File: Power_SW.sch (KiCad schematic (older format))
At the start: 96 parts, among them J9 2057-PH1-04-UA-ND, Q10 FDMS7608S, Q11 FDMS7608S, Q12 FDMS7608S, Q13 FDMS7608S, Q26 BC847BV, Q27 BC847BV, U35 XRP7724ILB-F, U36 NCP186AMX180TAG, U37 NCP186AMX120TAG

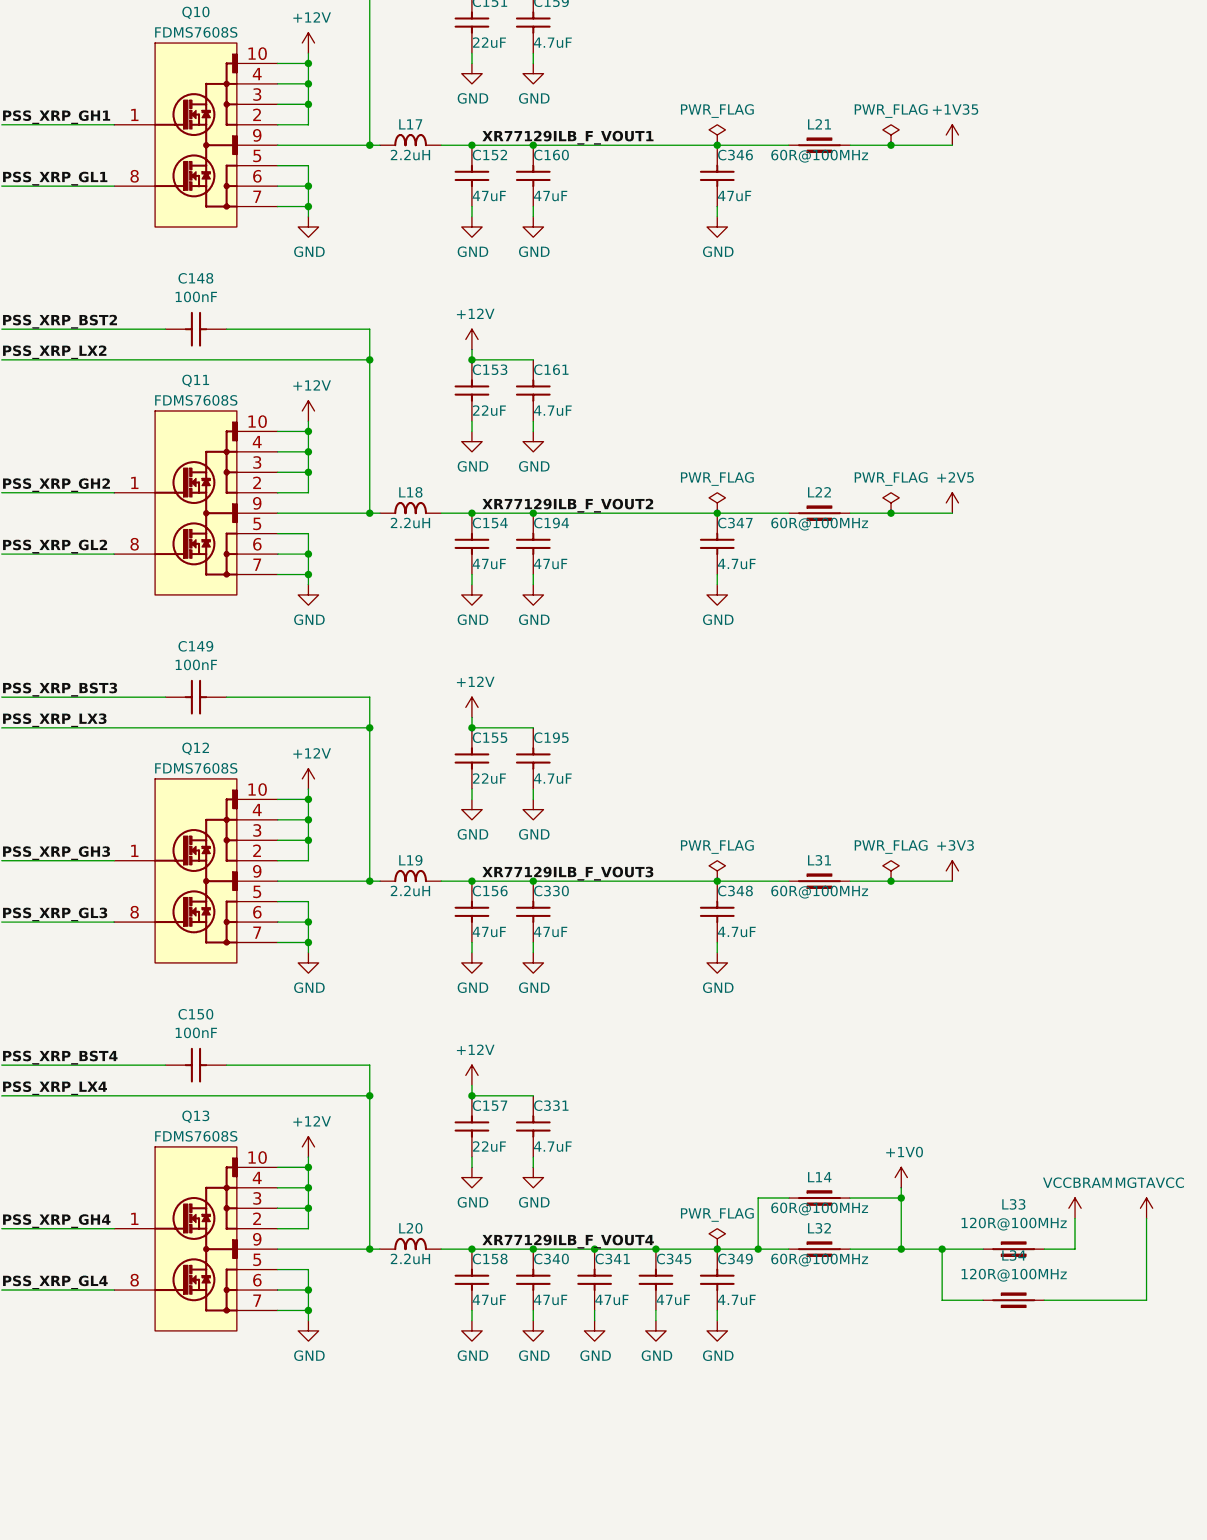
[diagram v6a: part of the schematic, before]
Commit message: added netlist to .xdc converter
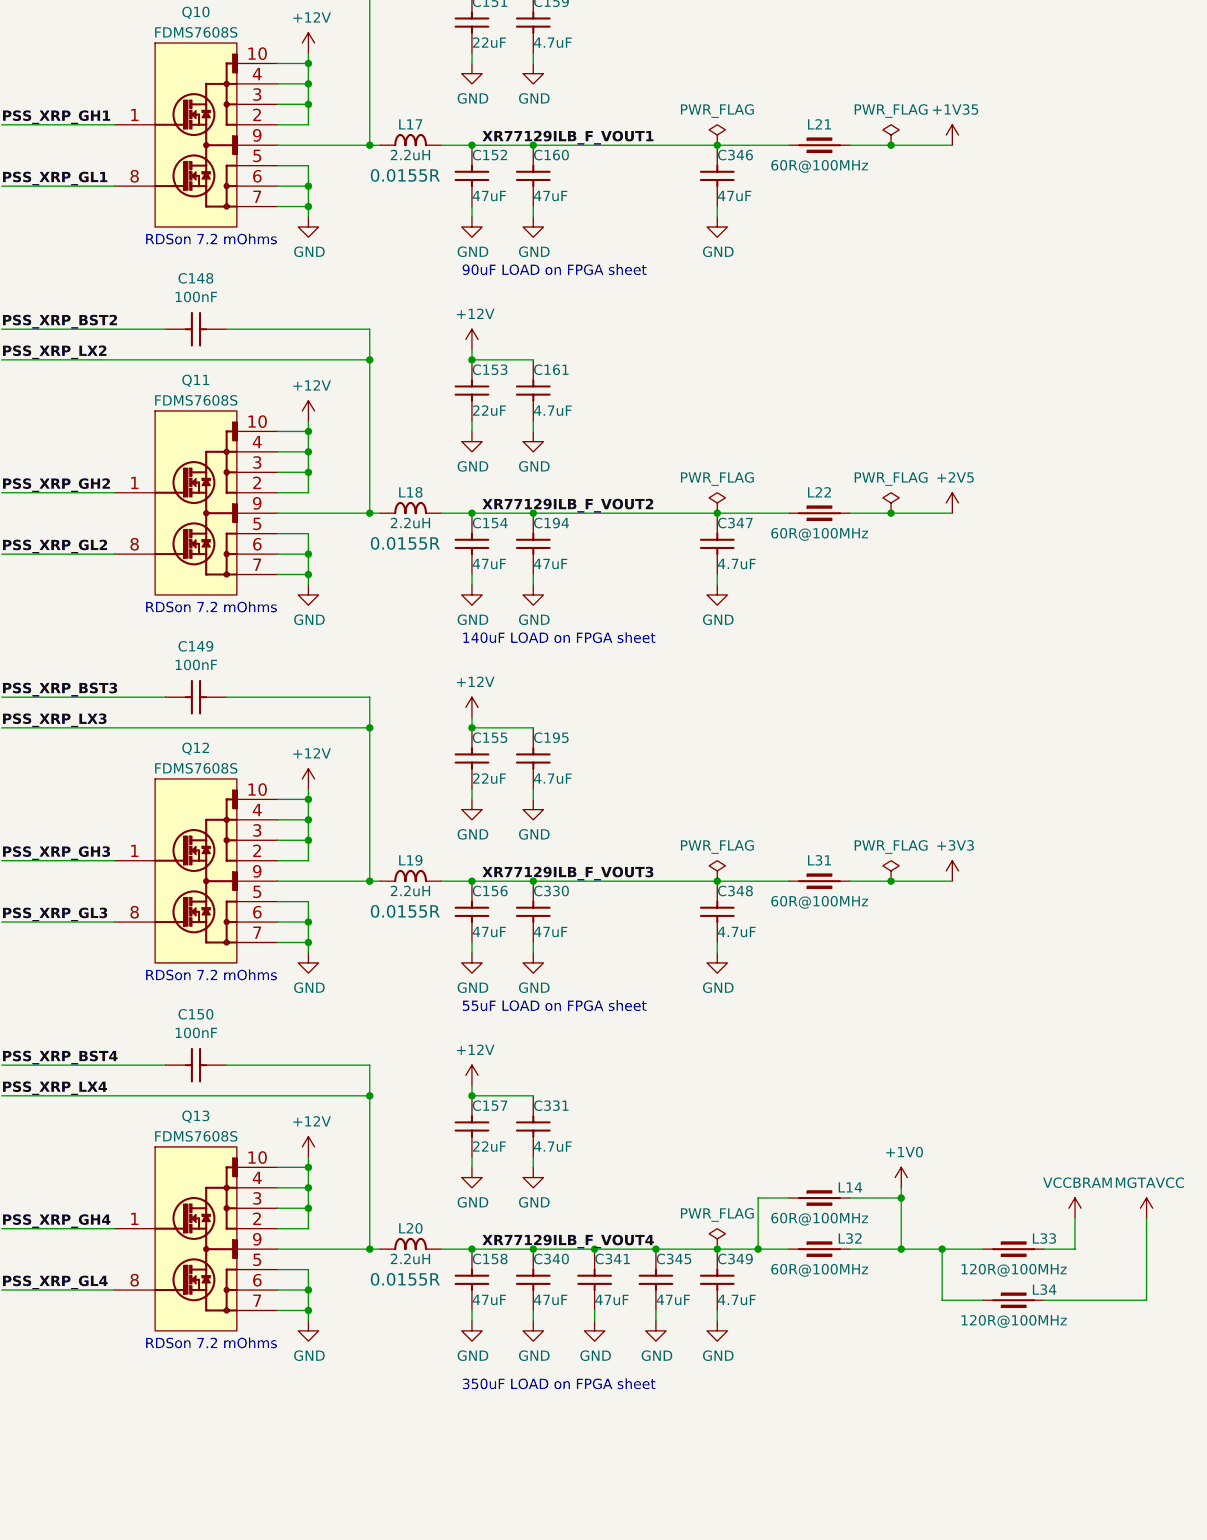
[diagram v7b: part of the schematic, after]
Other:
- note added: "140uF LOAD on FPGA sheet"
- note added: "350uF LOAD on FPGA sheet"
- note added: "55uF LOAD on FPGA sheet"
- note added: "90uF LOAD on FPGA sheet"
- note added: "RDSon 7.2 mOhms"
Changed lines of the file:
@@
 F 2 "INDC4516X180N" H 13900 1350 60  0001 L CNN
 F 3 "\\\\cern.ch\\dfs\\Applications\\Altium\\Datasheets\\IND1806_MURATA_BLM41P.pdf" H 13900 1980 60  0001 L CNN
-F 4 "60R@100MHz" H 14050 2300 50  0000 C CNN "~"
+F 4 "60R@100MHz" H 14050 2250 50  0000 C CNN "~"
 F 5 "IND1806_MURATA_BLM41PG600SN1L" H 13900 1890 60  0001 L CNN "Part Number"
 F 6 "Inductor" H 13900 1800 60  0001 L CNN "Library Ref"
@@
 U 1 1 5D0CD8A1
 P 14850 7750
-F 0 "L33" H 15000 7967 50  0000 C CNN
+F 0 "L33" H 15150 7800 50  0000 C CNN
 F 1 "IND0603_MURATA_BLM18SG121TN1D" H 14850 7560 60  0001 L CNN
 F 2 "INDC1608X65N" H 14850 6750 60  0001 L CNN
 F 3 "\\\\cern.ch\\dfs\\Applications\\Altium\\Datasheets\\IND0603_MURATA_BLM18S.pdf" H 14850 7380 60  0001 L CNN
-F 4 "120R@100MHz" H 15000 7876 50  0000 C CNN "~"
+F 4 "120R@100MHz" H 15000 7650 50  0000 C CNN "~"
 F 5 "IND0603_MURATA_BLM18SG121TN1D" H 14850 7290 60  0001 L CNN "Part Number"
 F 6 "Inductor" H 14850 7200 60  0001 L CNN "Library Ref"
@@
 U 1 1 5D0CDADB
 P 14850 8000
-F 0 "L34" H 15000 8217 50  0000 C CNN
+F 0 "L34" H 15150 8050 50  0000 C CNN
 F 1 "IND0603_MURATA_BLM18SG121TN1D" H 14850 7810 60  0001 L CNN
 F 2 "INDC1608X65N" H 14850 7000 60  0001 L CNN
 F 3 "\\\\cern.ch\\dfs\\Applications\\Altium\\Datasheets\\IND0603_MURATA_BLM18S.pdf" H 14850 7630 60  0001 L CNN
-F 4 "120R@100MHz" H 15000 8126 50  0000 C CNN "~"
+F 4 "120R@100MHz" H 15000 7900 50  0000 C CNN "~"
 F 5 "IND0603_MURATA_BLM18SG121TN1D" H 14850 7540 60  0001 L CNN "Part Number"
 F 6 "Inductor" H 14850 7450 60  0001 L CNN "Library Ref"
@@
 F 2 "INDC4516X180N" H 13900 3150 60  0001 L CNN
 F 3 "\\\\cern.ch\\dfs\\Applications\\Altium\\Datasheets\\IND1806_MURATA_BLM41P.pdf" H 13900 3780 60  0001 L CNN
-F 4 "60R@100MHz" H 14050 4100 50  0000 C CNN "~"
+F 4 "60R@100MHz" H 14050 4050 50  0000 C CNN "~"
 F 5 "IND1806_MURATA_BLM41PG600SN1L" H 13900 3690 60  0001 L CNN "Part Number"
 F 6 "Inductor" H 13900 3600 60  0001 L CNN "Library Ref"
@@
 F 2 "INDC4516X180N" H 13900 4950 60  0001 L CNN
 F 3 "\\\\cern.ch\\dfs\\Applications\\Altium\\Datasheets\\IND1806_MURATA_BLM41P.pdf" H 13900 5580 60  0001 L CNN
-F 4 "60R@100MHz" H 14050 5900 50  0000 C CNN "~"
+F 4 "60R@100MHz" H 14050 5850 50  0000 C CNN "~"
 F 5 "IND1806_MURATA_BLM41PG600SN1L" H 13900 5490 60  0001 L CNN "Part Number"
 F 6 "Inductor" H 13900 5400 60  0001 L CNN "Library Ref"
@@
 U 1 1 5D189CEC
 P 13900 7750
-F 0 "L32" H 14050 7850 50  0000 C CNN
+F 0 "L32" H 14200 7800 50  0000 C CNN
 F 1 "IND1806_MURATA_BLM41PG600SN1L" H 13900 7560 60  0001 L CNN
 F 2 "INDC4516X180N" H 13900 6750 60  0001 L CNN
 F 3 "\\\\cern.ch\\dfs\\Applications\\Altium\\Datasheets\\IND1806_MURATA_BLM41P.pdf" H 13900 7380 60  0001 L CNN
-F 4 "60R@100MHz" H 14050 7700 50  0000 C CNN "~"
+F 4 "60R@100MHz" H 14050 7650 50  0000 C CNN "~"
 F 5 "IND1806_MURATA_BLM41PG600SN1L" H 13900 7290 60  0001 L CNN "Part Number"
 F 6 "Inductor" H 13900 7200 60  0001 L CNN "Library Ref"
@@
 F 16 "None" H 11900 810 60  0001 L CNN "Status"
 F 17 "9A" H 11900 720 60  0001 L CNN "Power"
-F 18 "0.0155R" H 11900 630 60  0001 L CNN "Resistance"
+F 18 "0.0155R" H 11850 2200 60  0000 L CNN "Resistance"
 F 19 "±20%" H 11900 540 60  0001 L CNN "Tolerance"
 F 20 "Shielded SMD Power Inductor" H 11900 450 60  0001 L CNN "Part Description"
@@
 F 16 "None" H 11900 2610 60  0001 L CNN "Status"
 F 17 "9A" H 11900 2520 60  0001 L CNN "Power"
-F 18 "0.0155R" H 11900 2430 60  0001 L CNN "Resistance"
+F 18 "0.0155R" H 11850 4000 60  0000 L CNN "Resistance"
 F 19 "±20%" H 11900 2340 60  0001 L CNN "Tolerance"
 F 20 "Shielded SMD Power Inductor" H 11900 2250 60  0001 L CNN "Part Description"
@@
 F 16 "None" H 11900 4410 60  0001 L CNN "Status"
 F 17 "9A" H 11900 4320 60  0001 L CNN "Power"
-F 18 "0.0155R" H 11900 4230 60  0001 L CNN "Resistance"
+F 18 "0.0155R" H 11850 5800 60  0000 L CNN "Resistance"
 F 19 "±20%" H 11900 4140 60  0001 L CNN "Tolerance"
 F 20 "Shielded SMD Power Inductor" H 11900 4050 60  0001 L CNN "Part Description"
@@
 F 16 "None" H 11900 6210 60  0001 L CNN "Status"
 F 17 "9A" H 11900 6120 60  0001 L CNN "Power"
-F 18 "0.0155R" H 11900 6030 60  0001 L CNN "Resistance"
+F 18 "0.0155R" H 11850 7600 60  0000 L CNN "Resistance"
 F 19 "±20%" H 11900 5940 60  0001 L CNN "Tolerance"
 F 20 "Shielded SMD Power Inductor" H 11900 5850 60  0001 L CNN "Part Description"
@@
 U 1 1 5CF9305C
 P 13900 7500
-F 0 "L14" H 14050 7600 50  0000 C CNN
+F 0 "L14" H 14200 7550 50  0000 C CNN
 F 1 "IND1806_MURATA_BLM41PG600SN1L" H 13900 7310 60  0001 L CNN
 F 2 "INDC4516X180N" H 13900 6500 60  0001 L CNN
 F 3 "\\\\cern.ch\\dfs\\Applications\\Altium\\Datasheets\\IND1806_MURATA_BLM41P.pdf" H 13900 7130 60  0001 L CNN
-F 4 "60R@100MHz" H 14050 7450 50  0000 C CNN "~"
+F 4 "60R@100MHz" H 14050 7400 50  0000 C CNN "~"
 F 5 "IND1806_MURATA_BLM41PG600SN1L" H 13900 7040 60  0001 L CNN "Part Number"
 F 6 "Inductor" H 13900 6950 60  0001 L CNN "Library Ref"
@@
 Wire Wire Line
 	13750 7750 13900 7750
+Text Notes 12300 6600 0    50   ~ 0
+55uF LOAD on FPGA sheet
+Text Notes 12300 8450 0    50   ~ 0
+350uF LOAD on FPGA sheet
+Text Notes 12300 4800 0    50   ~ 0
+140uF LOAD on FPGA sheet
+Text Notes 12300 3000 0    50   ~ 0
+90uF LOAD on FPGA sheet
+Text Notes 10750 2850 0    50   ~ 0
+RDSon 7.2 mOhms
+Text Notes 10750 4650 0    50   ~ 0
+RDSon 7.2 mOhms
+Text Notes 10750 6450 0    50   ~ 0
+RDSon 7.2 mOhms
+Text Notes 10750 8250 0    50   ~ 0
+RDSon 7.2 mOhms
 $EndSCHEMATC
